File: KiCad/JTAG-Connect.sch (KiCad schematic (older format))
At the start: 2 parts, among them J1 Conn_02x05_Odd_Even, J2 Conn_02x03_Odd_Even

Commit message: updated design
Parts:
- removed J2: Conn_02x03_Odd_Even, Connector_PinHeader_2.00mm:PinHeader_2x03_P2.00mm_Vertical, symbol Connector_Generic:Conn_02x03_Odd_Even
- added J2, J3: Conn_02x05_Odd_Even, JTAG-Connect:PinHeader_2x05_P2.00mm_JTAG_connect_on_SMD_pads, symbol Connector_Generic:Conn_02x05_Odd_Even
- added J4: Conn_02x05_Odd_Even, Connector_IDC:IDC-Header_2x05_P2.54mm_Vertical, symbol Connector_Generic:Conn_02x05_Odd_Even
- added J5, J6: Conn_02x03_Odd_Even, JTAG-Connect:PinHeader_2x03_P2.00mm_JTAG_connect_on_SMD_pads, symbol Connector_Generic:Conn_02x03_Odd_Even
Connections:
- net GND: now also J2.10 (Pin_10), J2.2 (Pin_2), J4.10 (Pin_10), J4.2 (Pin_2), J5.2 (Pin_2)
- net TCK: now also J2.1 (Pin_1)
- net TDI: now also J2.9 (Pin_9)
- net TDO: now also J2.3 (Pin_3)
- net TMS: now also J2.5 (Pin_5)
- net Vtarget: now also J2.4 (Pin_4)
- new net TCK2: J4.1 (Pin_1), J5.1 (Pin_1)
- new net TDI2: J4.9 (Pin_9), J5.4 (Pin_4)
- new net TDO2: J4.3 (Pin_3), J5.3 (Pin_3)
- new net TMS2: J4.5 (Pin_5), J5.5 (Pin_5)
- new net Vtarget2: J4.4 (Pin_4), J5.6 (Pin_6)
- no-connect marks 3 -> 25
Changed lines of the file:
@@
 $EndDescr
-$Comp
-L Connector_Generic:Conn_02x03_Odd_Even J2
-U 1 1 6687D8BE
-P 3650 2650
-F 0 "J2" H 3700 2967 50  0000 C CNN
-F 1 "Conn_02x03_Odd_Even" H 3700 2876 50  0000 C CNN
-F 2 "Connector_PinHeader_2.00mm:PinHeader_2x03_P2.00mm_Vertical" H 3650 2650 50  0001 C CNN
-F 3 "~" H 3650 2650 50  0001 C CNN
-	1    3650 2650
-	1    0    0    -1
-$EndComp
-Text GLabel 3450 2550 0    50   Input ~ 0
-TCK
-Text GLabel 3450 2650 0    50   Input ~ 0
-TDO
-Text GLabel 3450 2750 0    50   Input ~ 0
-TMS
-Text GLabel 3950 2550 2    50   Input ~ 0
-GND
-Text GLabel 3950 2650 2    50   Input ~ 0
-TDI
-Text GLabel 3950 2750 2    50   Input ~ 0
-Vtarget
 $Comp
 L Connector_Generic:Conn_02x05_Odd_Even J1
@@
 TDI
 NoConn ~ 2150 2700
-Text GLabel 2650 2400 2    50   Input ~ 0
+NoConn ~ 2650 2600
+NoConn ~ 2650 2700
+$Comp
+L Connector_Generic:Conn_02x05_Odd_Even J2
+U 1 1 66A23D81
+P 3600 2600
+F 0 "J2" H 3650 3017 50  0000 C CNN
+F 1 "Conn_02x05_Odd_Even" H 3650 2926 50  0000 C CNN
+F 2 "JTAG-Connect:PinHeader_2x05_P2.00mm_JTAG_connect_on_SMD_pads" H 3600 2600 50  0001 C CNN
+F 3 "~" H 3600 2600 50  0001 C CNN
+	1    3600 2600
+	1    0    0    -1
+$EndComp
+Text GLabel 3400 2400 0    50   Input ~ 0
+TCK
+Text GLabel 3400 2500 0    50   Input ~ 0
+TDO
+Text GLabel 3400 2600 0    50   Input ~ 0
+TMS
+Text GLabel 3400 2800 0    50   Input ~ 0
+TDI
+Text GLabel 2650 2800 2    50   Input ~ 0
 GND
 Text GLabel 2650 2500 2    50   Input ~ 0
 Vtarget
-Text GLabel 2650 2800 2    50   Input ~ 0
+Text GLabel 2650 2400 2    50   Input ~ 0
 GND
-NoConn ~ 2650 2600
-NoConn ~ 2650 2700
+Text GLabel 3900 2800 2    50   Input ~ 0
+GND
+Text GLabel 3900 2500 2    50   Input ~ 0
+Vtarget
+Text GLabel 3900 2400 2    50   Input ~ 0
+GND
+NoConn ~ 3400 2700
+NoConn ~ 3900 2600
+NoConn ~ 3900 2700
+$Comp
+L Connector_Generic:Conn_02x05_Odd_Even J3
+U 1 1 66A4E5A1
+P 4850 2600
+F 0 "J3" H 4900 3017 50  0000 C CNN
+F 1 "Conn_02x05_Odd_Even" H 4900 2926 50  0000 C CNN
+F 2 "JTAG-Connect:PinHeader_2x05_P2.00mm_JTAG_connect_on_SMD_pads" H 4850 2600 50  0001 C CNN
+F 3 "~" H 4850 2600 50  0001 C CNN
+	1    4850 2600
+	1    0    0    -1
+$EndComp
+NoConn ~ 4650 2700
+NoConn ~ 5150 2600
+NoConn ~ 5150 2700
+NoConn ~ 4650 2400
+NoConn ~ 4650 2500
+NoConn ~ 4650 2600
+NoConn ~ 4650 2800
+NoConn ~ 5150 2500
+NoConn ~ 5150 2800
+NoConn ~ 5150 2400
+$Comp
+L Connector_Generic:Conn_02x03_Odd_Even J5
+U 1 1 66A79AD5
+P 3600 3450
+F 0 "J5" H 3650 3767 50  0000 C CNN
+F 1 "Conn_02x03_Odd_Even" H 3650 3676 50  0000 C CNN
+F 2 "JTAG-Connect:PinHeader_2x03_P2.00mm_JTAG_connect_on_SMD_pads" H 3600 3450 50  0001 C CNN
+F 3 "~" H 3600 3450 50  0001 C CNN
+	1    3600 3450
+	1    0    0    -1
+$EndComp
+Text GLabel 3400 3350 0    50   Input ~ 0
+TCK2
+Text GLabel 3400 3450 0    50   Input ~ 0
+TDO2
+Text GLabel 3400 3550 0    50   Input ~ 0
+TMS2
+Text GLabel 3900 3350 2    50   Input ~ 0
+GND
+Text GLabel 3900 3450 2    50   Input ~ 0
+TDI2
+NoConn ~ 5150 3550
+NoConn ~ 4650 3350
+NoConn ~ 4650 3450
+NoConn ~ 4650 3550
+NoConn ~ 5150 3450
+NoConn ~ 5150 3350
+Text GLabel 3900 3550 2    50   Input ~ 0
+Vtarget2
+$Comp
+L Connector_Generic:Conn_02x05_Odd_Even J4
+U 1 1 66A89D27
+P 2350 3550
+F 0 "J4" H 2400 3967 50  0000 C CNN
+F 1 "Conn_02x05_Odd_Even" H 2400 3876 50  0000 C CNN
+F 2 "Connector_IDC:IDC-Header_2x05_P2.54mm_Vertical" H 2350 3550 50  0001 C CNN
+F 3 "~" H 2350 3550 50  0001 C CNN
+	1    2350 3550
+	1    0    0    -1
+$EndComp
+Text GLabel 2150 3750 0    50   Input ~ 0
+TDI2
+NoConn ~ 2150 3650
+NoConn ~ 2650 3550
+NoConn ~ 2650 3650
+Text GLabel 2650 3750 2    50   Input ~ 0
+GND
+Text GLabel 2650 3450 2    50   Input ~ 0
+Vtarget2
+Text GLabel 2650 3350 2    50   Input ~ 0
+GND
+Text GLabel 2150 3350 0    50   Input ~ 0
+TCK2
+Text GLabel 2150 3450 0    50   Input ~ 0
+TDO2
+Text GLabel 2150 3550 0    50   Input ~ 0
+TMS2
+$Comp
+L Connector_Generic:Conn_02x03_Odd_Even J6
+U 1 1 66A98FAE
+P 4850 3450
+F 0 "J6" H 4900 3767 50  0000 C CNN
+F 1 "Conn_02x03_Odd_Even" H 4900 3676 50  0000 C CNN
+F 2 "JTAG-Connect:PinHeader_2x03_P2.00mm_JTAG_connect_on_SMD_pads" H 4850 3450 50  0001 C CNN
+F 3 "~" H 4850 3450 50  0001 C CNN
+	1    4850 3450
+	1    0    0    -1
+$EndComp
 $EndSCHEMATC

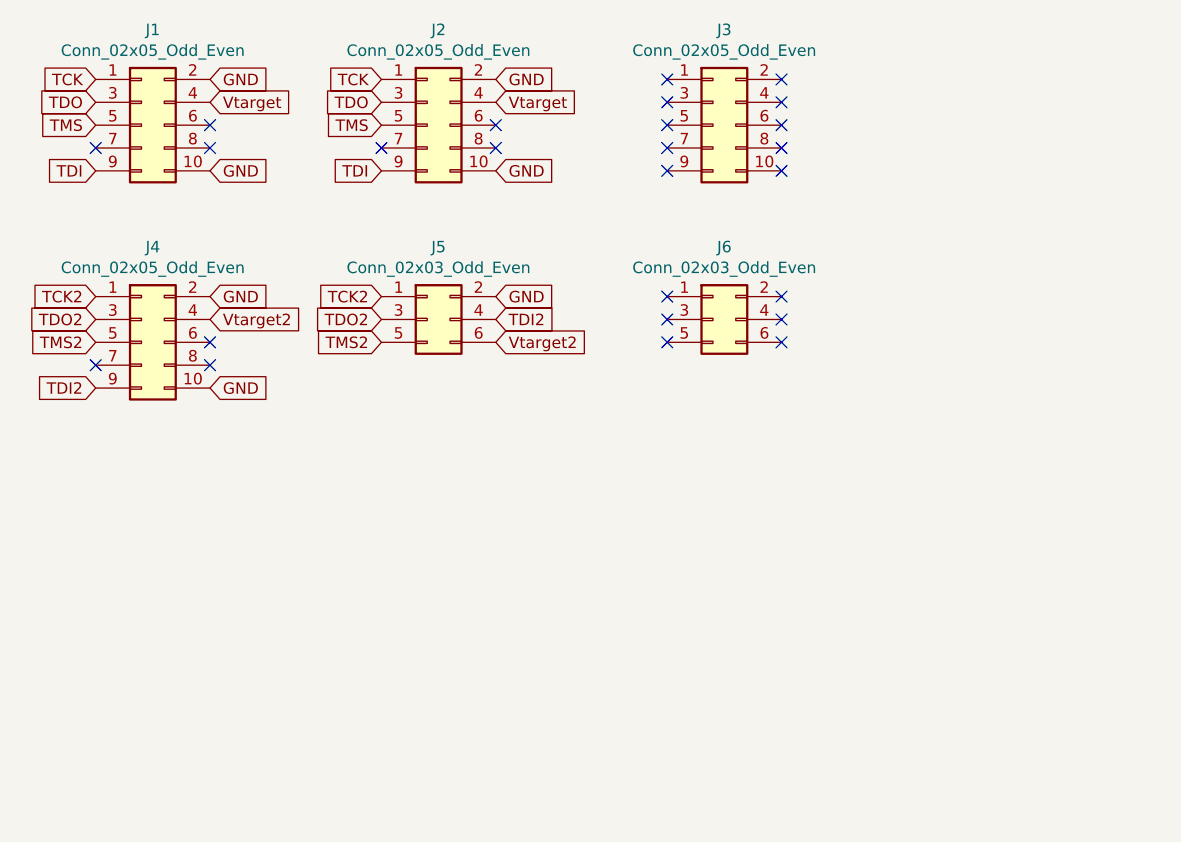
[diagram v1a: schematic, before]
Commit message: Updated design to fit DIY spring clip.
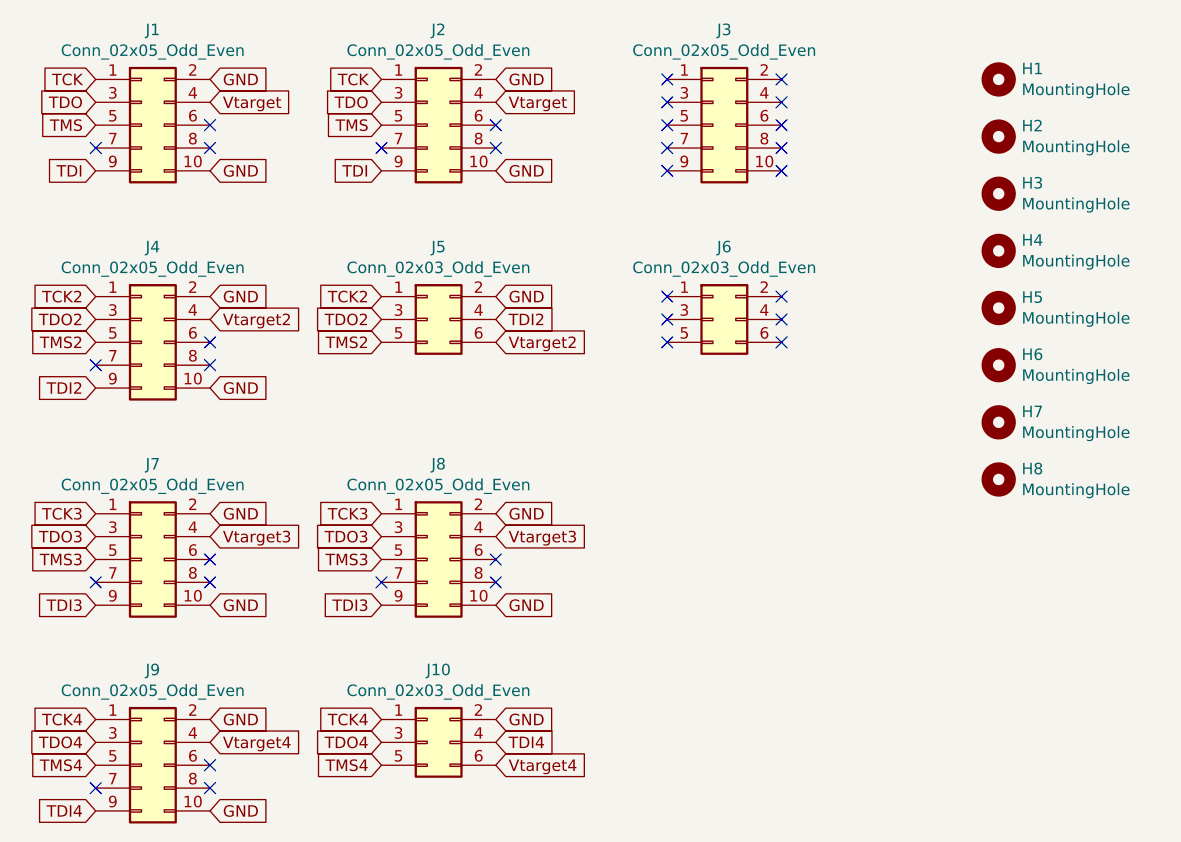
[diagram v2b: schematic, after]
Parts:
- added H1, H2, H3, H4, H5, H6, H7, H8: MountingHole, MountingHole:MountingHole_2mm, symbol Mechanical:MountingHole
- added J10: Conn_02x03_Odd_Even, JTAG-Connect:PinHeader_2x03_P2.00mm_JTAG_connect_on_SMD_pads, symbol Connector_Generic:Conn_02x03_Odd_Even
- added J7, J9: Conn_02x05_Odd_Even, Connector_IDC:IDC-Header_2x05_P2.54mm_Vertical, symbol Connector_Generic:Conn_02x05_Odd_Even
- added J8: Conn_02x05_Odd_Even, JTAG-Connect:PinHeader_2x05_P2.00mm_JTAG_connect_on_SMD_pads, symbol Connector_Generic:Conn_02x05_Odd_Even
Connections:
- net GND: now also J10.2 (Pin_2), J7.10 (Pin_10), J7.2 (Pin_2), J8.10 (Pin_10), J8.2 (Pin_2), J9.10 (Pin_10), J9.2 (Pin_2)
- new net TCK3: J7.1 (Pin_1), J8.1 (Pin_1)
- new net TCK4: J10.1 (Pin_1), J9.1 (Pin_1)
- new net TDI3: J7.9 (Pin_9), J8.9 (Pin_9)
- new net TDI4: J10.4 (Pin_4), J9.9 (Pin_9)
- new net TDO3: J7.3 (Pin_3), J8.3 (Pin_3)
- new net TDO4: J10.3 (Pin_3), J9.3 (Pin_3)
- new net TMS3: J7.5 (Pin_5), J8.5 (Pin_5)
- new net TMS4: J10.5 (Pin_5), J9.5 (Pin_5)
- new net Vtarget3: J7.4 (Pin_4), J8.4 (Pin_4)
- new net Vtarget4: J10.6 (Pin_6), J9.4 (Pin_4)
- no-connect marks 25 -> 34
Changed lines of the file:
@@
+	1    0    0    -1
+$EndComp
+$Comp
+L Mechanical:MountingHole H1
+U 1 1 66B33AAC
+P 6100 2400
+F 0 "H1" H 6200 2446 50  0000 L CNN
+F 1 "MountingHole" H 6200 2355 50  0000 L CNN
+F 2 "MountingHole:MountingHole_2mm" H 6100 2400 50  0001 C CNN
+F 3 "~" H 6100 2400 50  0001 C CNN
+	1    6100 2400
+	1    0    0    -1
+$EndComp
+$Comp
+L Mechanical:MountingHole H2
+U 1 1 66B342D5
+P 6100 2650
+F 0 "H2" H 6200 2696 50  0000 L CNN
+F 1 "MountingHole" H 6200 2605 50  0000 L CNN
+F 2 "MountingHole:MountingHole_2mm" H 6100 2650 50  0001 C CNN
+F 3 "~" H 6100 2650 50  0001 C CNN
+	1    6100 2650
+	1    0    0    -1
+$EndComp
+$Comp
+L Mechanical:MountingHole H3
+U 1 1 66B60B72
+P 6100 2900
+F 0 "H3" H 6200 2946 50  0000 L CNN
+F 1 "MountingHole" H 6200 2855 50  0000 L CNN
+F 2 "MountingHole:MountingHole_2mm" H 6100 2900 50  0001 C CNN
+F 3 "~" H 6100 2900 50  0001 C CNN
+	1    6100 2900
+	1    0    0    -1
+$EndComp
+$Comp
+L Mechanical:MountingHole H4
+U 1 1 66B60B7C
+P 6100 3150
+F 0 "H4" H 6200 3196 50  0000 L CNN
+F 1 "MountingHole" H 6200 3105 50  0000 L CNN
+F 2 "MountingHole:MountingHole_2mm" H 6100 3150 50  0001 C CNN
+F 3 "~" H 6100 3150 50  0001 C CNN
+	1    6100 3150
+	1    0    0    -1
+$EndComp
+$Comp
+L Mechanical:MountingHole H5
+U 1 1 66B66FB1
+P 6100 3400
+F 0 "H5" H 6200 3446 50  0000 L CNN
+F 1 "MountingHole" H 6200 3355 50  0000 L CNN
+F 2 "MountingHole:MountingHole_2mm" H 6100 3400 50  0001 C CNN
+F 3 "~" H 6100 3400 50  0001 C CNN
+	1    6100 3400
+	1    0    0    -1
+$EndComp
+$Comp
+L Mechanical:MountingHole H6
+U 1 1 66B66FBB
+P 6100 3650
+F 0 "H6" H 6200 3696 50  0000 L CNN
+F 1 "MountingHole" H 6200 3605 50  0000 L CNN
+F 2 "MountingHole:MountingHole_2mm" H 6100 3650 50  0001 C CNN
+F 3 "~" H 6100 3650 50  0001 C CNN
+	1    6100 3650
+	1    0    0    -1
+$EndComp
+$Comp
+L Mechanical:MountingHole H7
+U 1 1 66B7756F
+P 6100 3900
+F 0 "H7" H 6200 3946 50  0000 L CNN
+F 1 "MountingHole" H 6200 3855 50  0000 L CNN
+F 2 "MountingHole:MountingHole_2mm" H 6100 3900 50  0001 C CNN
+F 3 "~" H 6100 3900 50  0001 C CNN
+	1    6100 3900
+	1    0    0    -1
+$EndComp
+$Comp
+L Mechanical:MountingHole H8
+U 1 1 66B77579
+P 6100 4150
+F 0 "H8" H 6200 4196 50  0000 L CNN
+F 1 "MountingHole" H 6200 4105 50  0000 L CNN
+F 2 "MountingHole:MountingHole_2mm" H 6100 4150 50  0001 C CNN
+F 3 "~" H 6100 4150 50  0001 C CNN
+	1    6100 4150
+	1    0    0    -1
+$EndComp
+$Comp
+L Connector_Generic:Conn_02x05_Odd_Even J7
+U 1 1 66B7BC8C
+P 2350 4500
+F 0 "J7" H 2400 4917 50  0000 C CNN
+F 1 "Conn_02x05_Odd_Even" H 2400 4826 50  0000 C CNN
+F 2 "Connector_IDC:IDC-Header_2x05_P2.54mm_Vertical" H 2350 4500 50  0001 C CNN
+F 3 "~" H 2350 4500 50  0001 C CNN
+	1    2350 4500
+	1    0    0    -1
+$EndComp
+Text GLabel 2150 4300 0    50   Input ~ 0
+TCK3
+Text GLabel 2150 4400 0    50   Input ~ 0
+TDO3
+Text GLabel 2150 4500 0    50   Input ~ 0
+TMS3
+Text GLabel 2150 4700 0    50   Input ~ 0
+TDI3
+NoConn ~ 2150 4600
+NoConn ~ 2650 4500
+NoConn ~ 2650 4600
+$Comp
+L Connector_Generic:Conn_02x05_Odd_Even J8
+U 1 1 66B7BC9D
+P 3600 4500
+F 0 "J8" H 3650 4917 50  0000 C CNN
+F 1 "Conn_02x05_Odd_Even" H 3650 4826 50  0000 C CNN
+F 2 "JTAG-Connect:PinHeader_2x05_P2.00mm_JTAG_connect_on_SMD_pads" H 3600 4500 50  0001 C CNN
+F 3 "~" H 3600 4500 50  0001 C CNN
+	1    3600 4500
+	1    0    0    -1
+$EndComp
+Text GLabel 3400 4300 0    50   Input ~ 0
+TCK3
+Text GLabel 3400 4400 0    50   Input ~ 0
+TDO3
+Text GLabel 3400 4500 0    50   Input ~ 0
+TMS3
+Text GLabel 3400 4700 0    50   Input ~ 0
+TDI3
+Text GLabel 2650 4700 2    50   Input ~ 0
+GND
+Text GLabel 2650 4400 2    50   Input ~ 0
+Vtarget3
+Text GLabel 2650 4300 2    50   Input ~ 0
+GND
+Text GLabel 3900 4700 2    50   Input ~ 0
+GND
+Text GLabel 3900 4400 2    50   Input ~ 0
+Vtarget3
+Text GLabel 3900 4300 2    50   Input ~ 0
+GND
+NoConn ~ 3400 4600
+NoConn ~ 3900 4500
+NoConn ~ 3900 4600
+$Comp
+L Connector_Generic:Conn_02x05_Odd_Even J9
+U 1 1 66B88994
+P 2350 5400
+F 0 "J9" H 2400 5817 50  0000 C CNN
+F 1 "Conn_02x05_Odd_Even" H 2400 5726 50  0000 C CNN
+F 2 "Connector_IDC:IDC-Header_2x05_P2.54mm_Vertical" H 2350 5400 50  0001 C CNN
+F 3 "~" H 2350 5400 50  0001 C CNN
+	1    2350 5400
+	1    0    0    -1
+$EndComp
+Text GLabel 2150 5200 0    50   Input ~ 0
+TCK4
+Text GLabel 2150 5300 0    50   Input ~ 0
+TDO4
+Text GLabel 2150 5400 0    50   Input ~ 0
+TMS4
+Text GLabel 2150 5600 0    50   Input ~ 0
+TDI4
+NoConn ~ 2150 5500
+NoConn ~ 2650 5400
+NoConn ~ 2650 5500
+Text GLabel 3400 5200 0    50   Input ~ 0
+TCK4
+Text GLabel 3400 5300 0    50   Input ~ 0
+TDO4
+Text GLabel 3400 5400 0    50   Input ~ 0
+TMS4
+Text GLabel 3900 5300 2    50   Input ~ 0
+TDI4
+Text GLabel 2650 5600 2    50   Input ~ 0
+GND
+Text GLabel 2650 5300 2    50   Input ~ 0
+Vtarget4
+Text GLabel 2650 5200 2    50   Input ~ 0
+GND
+Text GLabel 3900 5400 2    50   Input ~ 0
+Vtarget4
+Text GLabel 3900 5200 2    50   Input ~ 0
+GND
+$Comp
+L Connector_Generic:Conn_02x03_Odd_Even J10
+U 1 1 66B8E629
+P 3600 5300
+F 0 "J10" H 3650 5617 50  0000 C CNN
+F 1 "Conn_02x03_Odd_Even" H 3650 5526 50  0000 C CNN
+F 2 "JTAG-Connect:PinHeader_2x03_P2.00mm_JTAG_connect_on_SMD_pads" H 3600 5300 50  0001 C CNN
+F 3 "~" H 3600 5300 50  0001 C CNN
+	1    3600 5300
 	1    0    0    -1
 $EndComp
